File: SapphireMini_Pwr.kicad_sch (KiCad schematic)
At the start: 33 parts, among them IC501 SLG59M1446V, J501 JST, Q501 BC857BS, Q502 IRLML6402TRPBF, U501 TPS62150

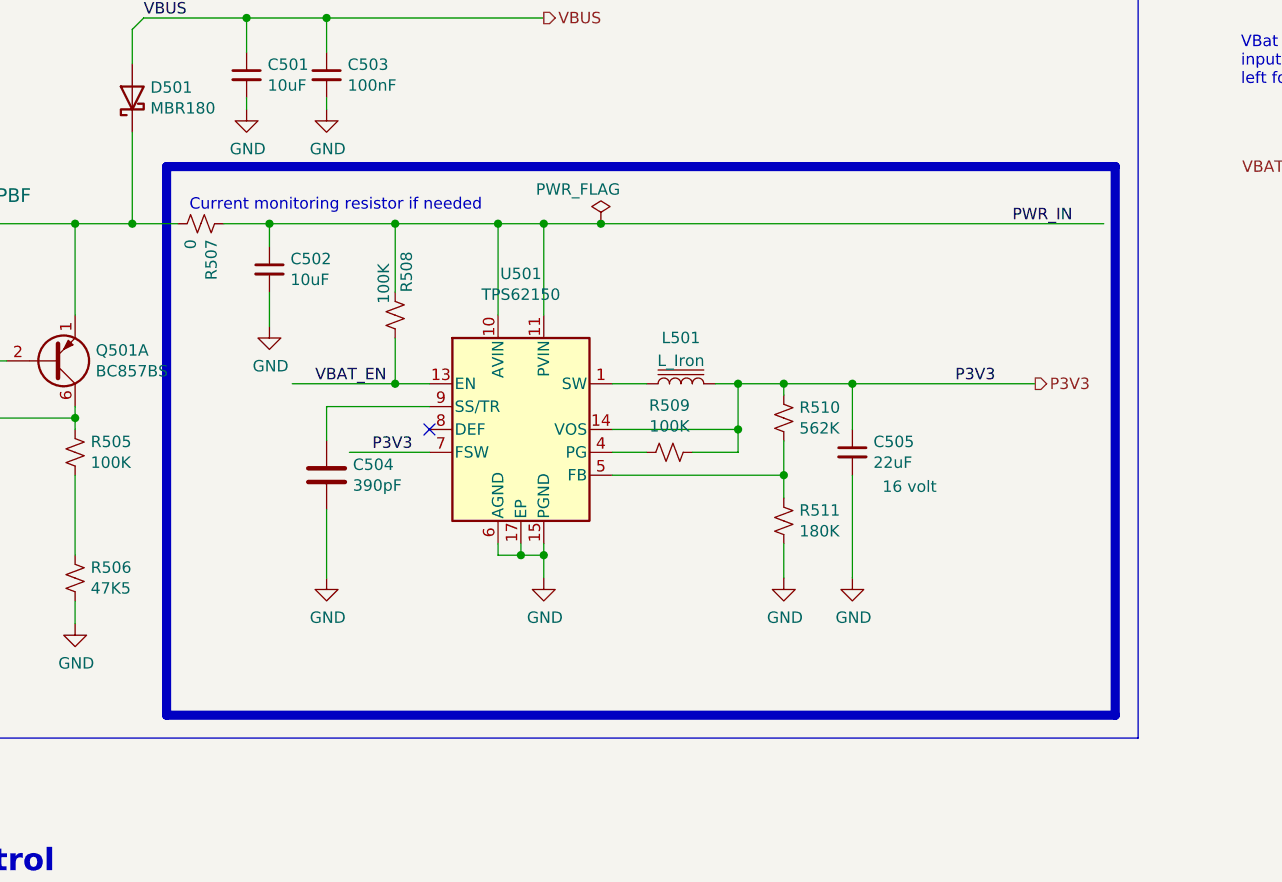
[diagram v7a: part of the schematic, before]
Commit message: Skematic updated for power and 1PSI sensor
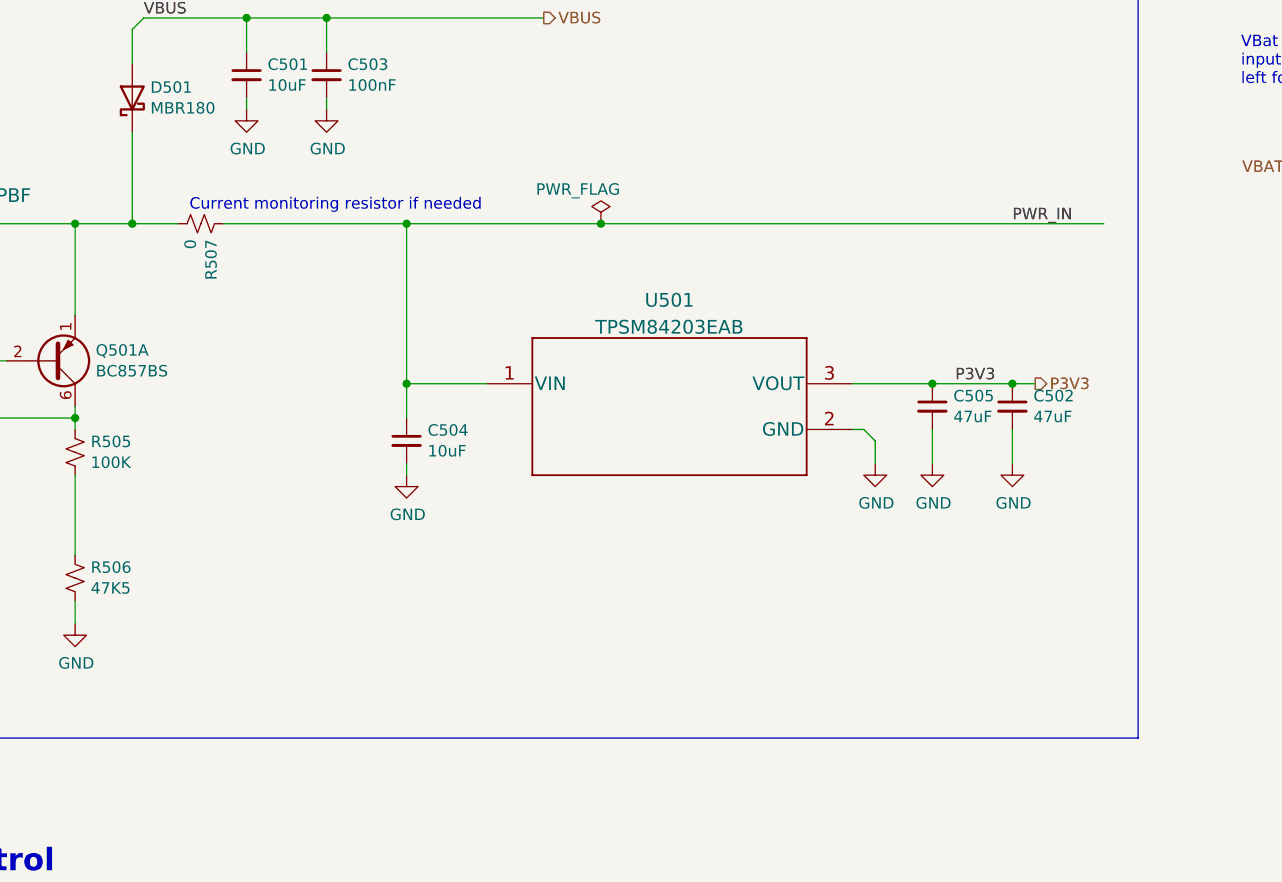
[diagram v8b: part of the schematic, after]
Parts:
- removed C504: 390pF, Capacitor_SMD:C_0603_1608Metric, symbol Device:C
- removed L501: L_Iron, SapphineMinimal:74439344022, symbol Device:L_Iron
- removed R508, R509: 100K, Resistor_SMD:R_0603_1608Metric, symbol Device:R_Small_US
- removed R510: 562K, Resistor_SMD:R_0603_1608Metric, symbol Device:R_Small_US
- removed R511: 180K, Resistor_SMD:R_0603_1608Metric, symbol Device:R_Small_US
- removed U501: TPS62150, Package_DFN_QFN:VQFN-16-1EP_3x3mm_P0.5mm_EP1.68x1.68mm_ThermalVias, symbol Regulator_Switching:TPS62150
- added C504: 10uF, Capacitor_SMD:C_1210_3225Metric, symbol Device:C_Small
- added U501: TPSM84203EAB, Sapphire:TPSM84203EAB, symbol sapphireMini:TPSM84203EAB
- C502: value 10uF -> 47uF; footprint Capacitor_SMD:C_0805_2012Metric -> Capacitor_SMD:C_1210_3225Metric; MPN CL21A106KAYNNNE -> CL32A476KOJNNNE
- C505: value 22uF -> 47uF; footprint Capacitor_SMD:C_1206_3216Metric -> Capacitor_SMD:C_1210_3225Metric; DPN 1276-2728-1-ND -> 490-10748-1-ND; Digi-Key_PN 445-12847-1-ND -> 490-10748-1-ND; DigiKey Price 0.42 -> (none); MPN CL21A226MAYNNNE -> CL32A476KOJNNNE; MacroFab_PN CC1206ZKY5V7BB226 -> (none); Manufacturer Samsung -> Samsung Electro-Mechanics; Tolerance 20% -> (none)
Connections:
- net GND: now also C504.2, U501.2 (GND)
- net P3V3: now also C502.1, U501.3 (VOUT)
- net PWR_IN: now also C504.1, U501.1 (VIN); no longer C502.1
- no-connect marks 3 -> 2
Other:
- moved on the sheet: C502
